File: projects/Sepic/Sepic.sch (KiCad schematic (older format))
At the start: 49 parts, among them CON1 USB-MINI-B-Vert, P1 V_in+, P10 V_out+, P11 V_out-, P12 GND, P13 GND, P14 GND, P15 V_in+, P16 V_in+, P17 GND, P18 V_in+, P19 V_in-, P2 GND, P20 V_out+, P21 V_out-, P22 V_out+, P23 V_out+, P24 GND, P25 GND, P26 V_out+, P27 V_out+, P28 GND, P29 GND, P3 JST_In, P30 CONN_3X2, P31 CONN_3X2, P32 CONN_2, P33 CONN_2, P4 V_in+, P5 V_in+, P6 V_in-, P7 V_in+, P8 V_out+, P9 GND, U1 LT1370

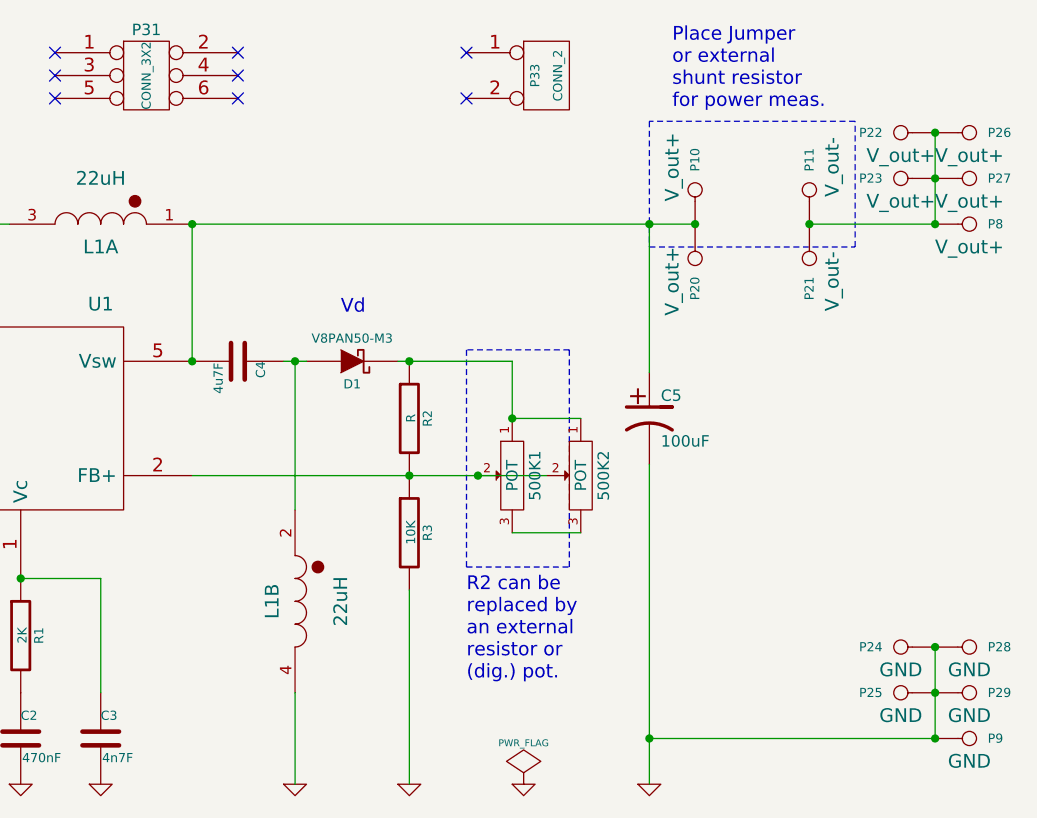
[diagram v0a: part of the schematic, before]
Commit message: schematic changed
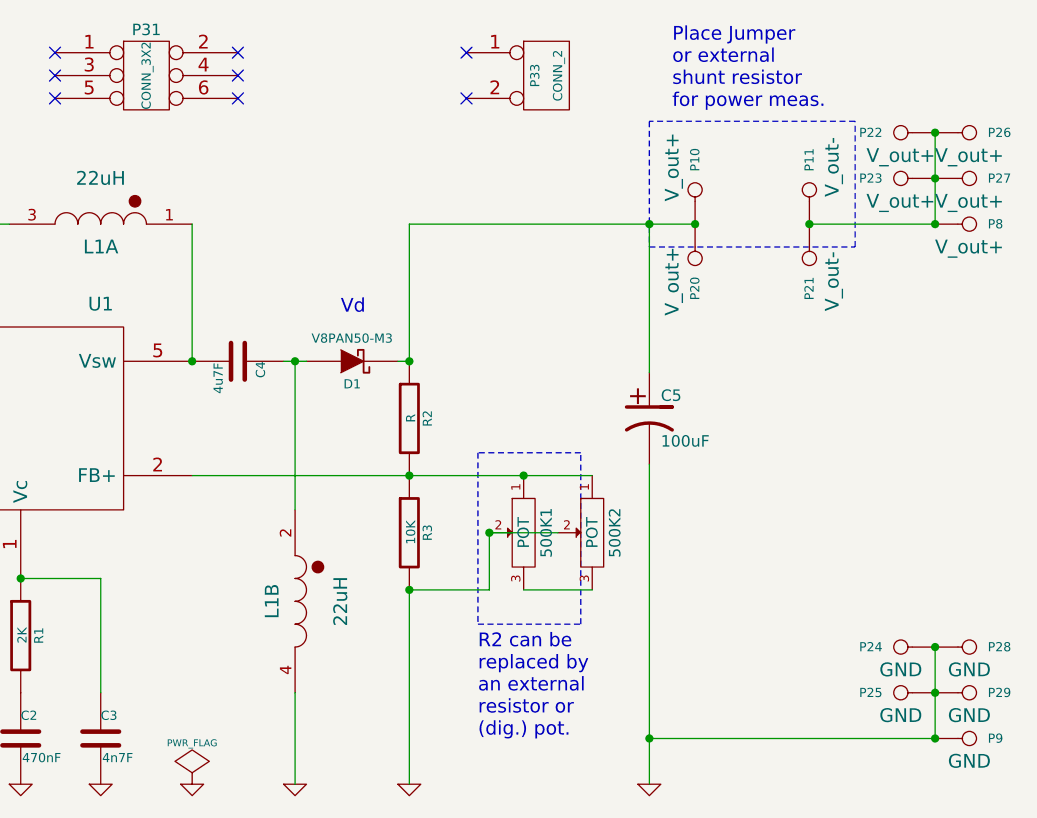
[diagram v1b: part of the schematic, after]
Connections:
- net GND: now also 500K1.2, 500K2.2
- net at C4.2, L1.1, U1.5 (Vsw): no longer C5.1, P10.1, P20.1
- net at D1.2 (K), R2.1: now also C5.1, P10.1, P20.1; no longer 500K1.1, 500K2.1
- net at R2.2, R3.1, U1.2 (FB+): now also 500K1.1, 500K2.1; no longer 500K1.2, 500K2.2
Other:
- moved on the sheet: 500K1, 500K2
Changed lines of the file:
@@
 Wire Wire Line
 	5050 4300 5050 5200
-Wire Wire Line
-	6300 3850 7850 3850
 Connection ~ 7250 3850
-Wire Wire Line
-	7200 3350 7700 3350
 Wire Wire Line
 	6700 3350 6800 3350
@@
 Wire Wire Line
 	8300 2750 8300 3400
-Connection ~ 6300 2750
 Wire Wire Line
 	8300 3800 8300 5200
@@
 L PWR_FLAG #FLG09
 U 1 1 55E95355
-P 7750 5200
-F 0 "#FLG09" H 7750 5295 30  0001 C CNN
-F 1 "PWR_FLAG" H 7750 5380 30  0000 C CNN
-F 2 "" H 7750 5200 60  0000 C CNN
-F 3 "" H 7750 5200 60  0000 C CNN
-	1    7750 5200
+P 6300 5200
+F 0 "#FLG09" H 6300 5295 30  0001 C CNN
+F 1 "PWR_FLAG" H 6300 5380 30  0000 C CNN
+F 2 "" H 6300 5200 60  0000 C CNN
+F 3 "" H 6300 5200 60  0000 C CNN
+	1    6300 5200
 	1    0    0    -1
 $EndComp
@@
 L GND #PWR010
 U 1 1 55E954C8
-P 7750 5200
-F 0 "#PWR010" H 7750 5200 30  0001 C CNN
-F 1 "GND" H 7750 5130 30  0001 C CNN
-F 2 "" H 7750 5200 60  0000 C CNN
-F 3 "" H 7750 5200 60  0000 C CNN
-	1    7750 5200
+P 6300 5200
+F 0 "#PWR010" H 6300 5200 30  0001 C CNN
+F 1 "GND" H 6300 5130 30  0001 C CNN
+F 2 "" H 6300 5200 60  0000 C CNN
+F 3 "" H 6300 5200 60  0000 C CNN
+	1    6300 5200
 	1    0    0    -1
 $EndComp
@@
 Text Notes 3550 5250 0    60   ~ 0
 Enable signal (S/S) \nfrom input with \nsolder jumper or \nexternal from P32
-Text Notes 7500 4750 0    60   ~ 0
+Text Notes 7550 5000 0    60   ~ 0
 R2 can be \nreplaced by \nan external \nresistor or \n(dig.) pot.
 $Comp
@@
 L POT 500K1
 U 1 1 55EA1D69
-P 7700 3850
-F 0 "500K1" H 7700 3750 50  0000 C CNN
-F 1 "POT" H 7700 3850 50  0000 C CNN
-F 2 "frep:Trimmer" H 7700 3850 60  0001 C CNN
-F 3 "" H 7700 3850 60  0000 C CNN
-	1    7700 3850
+P 7750 4100
+F 0 "500K1" H 7750 4000 50  0000 C CNN
+F 1 "POT" H 7750 4100 50  0000 C CNN
+F 2 "frep:Trimmer" H 7750 4100 60  0001 C CNN
+F 3 "" H 7750 4100 60  0000 C CNN
+	1    7750 4100
 	0    -1   1    0
 $EndComp
-Wire Wire Line
-	7700 3350 7700 3600
-Wire Notes Line
-	7500 3300 7500 4250
-Wire Notes Line
-	7500 4250 7950 4250
-Wire Notes Line
-	7950 4250 7950 3300
-Wire Notes Line
-	7950 3300 7500 3300
+Wire Notes Line
+	7550 3750 7550 4500
+Wire Notes Line
+	7550 4500 8000 4500
+Wire Notes Line
+	8000 4500 8000 3750
+Wire Notes Line
+	8000 3750 7550 3750
 $Comp
 L CP1 C5
@@
 	9200 2300 8300 2300
 Wire Wire Line
-	8300 5000 9550 5000
-Wire Wire Line
-	9000 2750 9550 2750
-Wire Wire Line
-	6300 2750 8500 2750
+	9550 5000 8300 5000
+Wire Wire Line
+	9550 2750 9000 2750
 Wire Wire Line
 	2100 3300 3100 3300
@@
 $EndComp
 Wire Wire Line
-	9550 2750 9550 2350
+	9550 2350 9550 2750
 Connection ~ 9550 2550
 Connection ~ 9550 2750
@@
 $EndComp
 Wire Wire Line
-	9550 5000 9550 4600
+	9550 4600 9550 5000
 Connection ~ 9550 4800
 Connection ~ 9550 5000
@@
 L POT 500K2
 U 1 1 56906635
-P 8000 3850
-F 0 "500K2" H 8000 3750 50  0000 C CNN
-F 1 "POT" H 8000 3850 50  0000 C CNN
-F 2 "frep:Trimmer" H 8000 3850 60  0001 C CNN
-F 3 "" H 8000 3850 60  0000 C CNN
-	1    8000 3850
+P 8050 4100
+F 0 "500K2" H 8050 4000 50  0000 C CNN
+F 1 "POT" H 8050 4100 50  0000 C CNN
+F 2 "frep:Trimmer" H 8050 4100 60  0001 C CNN
+F 3 "" H 8050 4100 60  0000 C CNN
+	1    8050 4100
 	0    -1   1    0
 $EndComp
 Wire Wire Line
-	7700 3600 8000 3600
-Connection ~ 7700 3600
-Connection ~ 7550 3850
+	6300 3850 8050 3850
+Connection ~ 7750 3850
+Connection ~ 7600 4100
 $Comp
 L CONN_3X2 P30
@@
 NoConn ~ 7500 2200
 Wire Wire Line
-	7700 4100 8000 4100
+	7750 4350 8050 4350
 Wire Wire Line
 	3800 4100 4100 4100
@@
 Text Notes 8400 2250 0    60   ~ 0
 Place Jumper \nor external\nshunt resistor\nfor power meas.
+Wire Wire Line
+	7200 3350 7250 3350
+Wire Wire Line
+	7600 4100 7600 4350
+Wire Wire Line
+	7600 4350 7250 4350
+Connection ~ 7250 4350
+Wire Wire Line
+	7250 3350 7250 2750
+Wire Wire Line
+	7250 2750 8500 2750
+Wire Wire Line
+	7900 4100 7600 4100
 $EndSCHEMATC

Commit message: Sepic updated
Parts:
- added R4: 10K, frep:R0805, symbol R
- added R5: 330R, frep:R0805, symbol R
- R2: value R -> 10K
- renumbered 500K1 to 20K1, 500K2 to 20K2
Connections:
- net GND: now also R4.2; no longer R3.2
- net at R2.2, R3.1, U1.2 (FB+): now also R5.2; no longer 20K1.1, 20K2.1
- new net: R3.2, R4.1
- new net: 20K1.1, 20K2.1, R5.1
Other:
- note added: "POT can be \nreplaced by \nan external \nresistor or \n(dig.) pot."
- note added: "R_p"
- note added: "V_out = V_ref * ( 1 + R2 / R_p )"
- note removed: "R2 can be \nreplaced by \nan external \nresistor or \n(dig.) pot."
- moved on the sheet: 20K1, 20K2, C1, C2, C3, C4, C5, CON1, D1, JP1, JP2, L1A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
